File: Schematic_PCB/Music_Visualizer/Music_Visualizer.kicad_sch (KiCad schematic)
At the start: 130 parts, among them U1 LM324, U4 LM324, U5 LM324, U6 LM324, U7 LM324, U8 LM324, U9 LM324

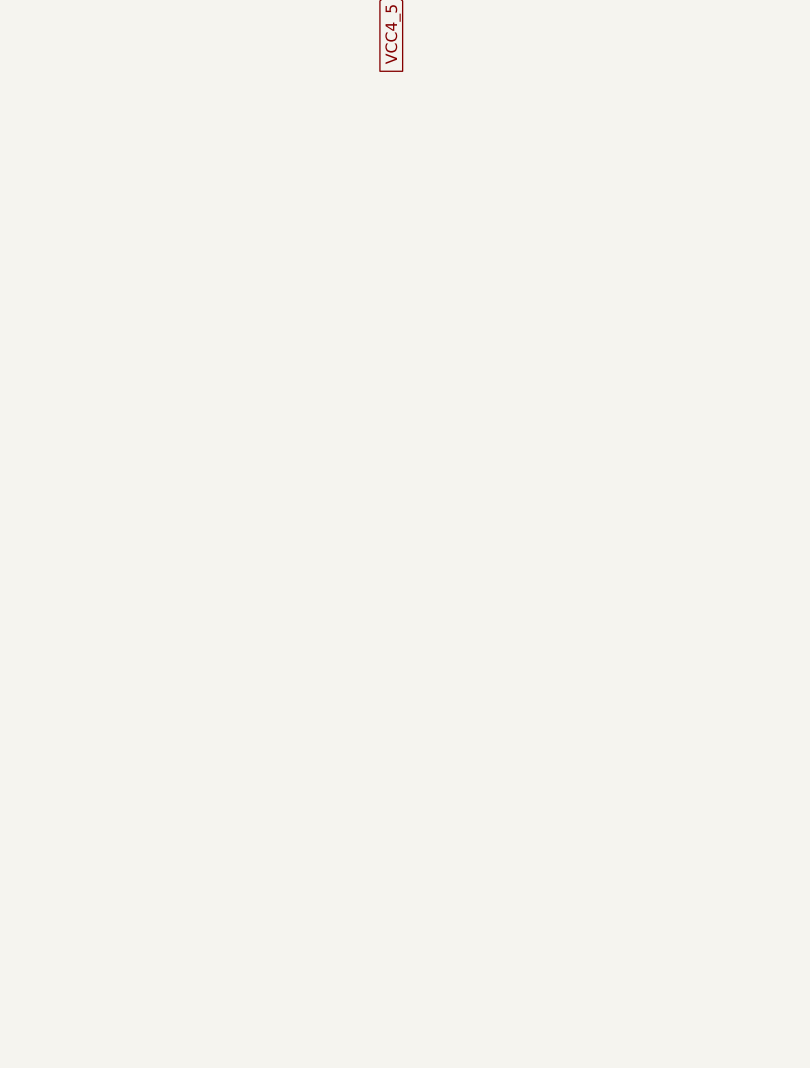
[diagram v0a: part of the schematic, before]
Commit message: Add testpoints
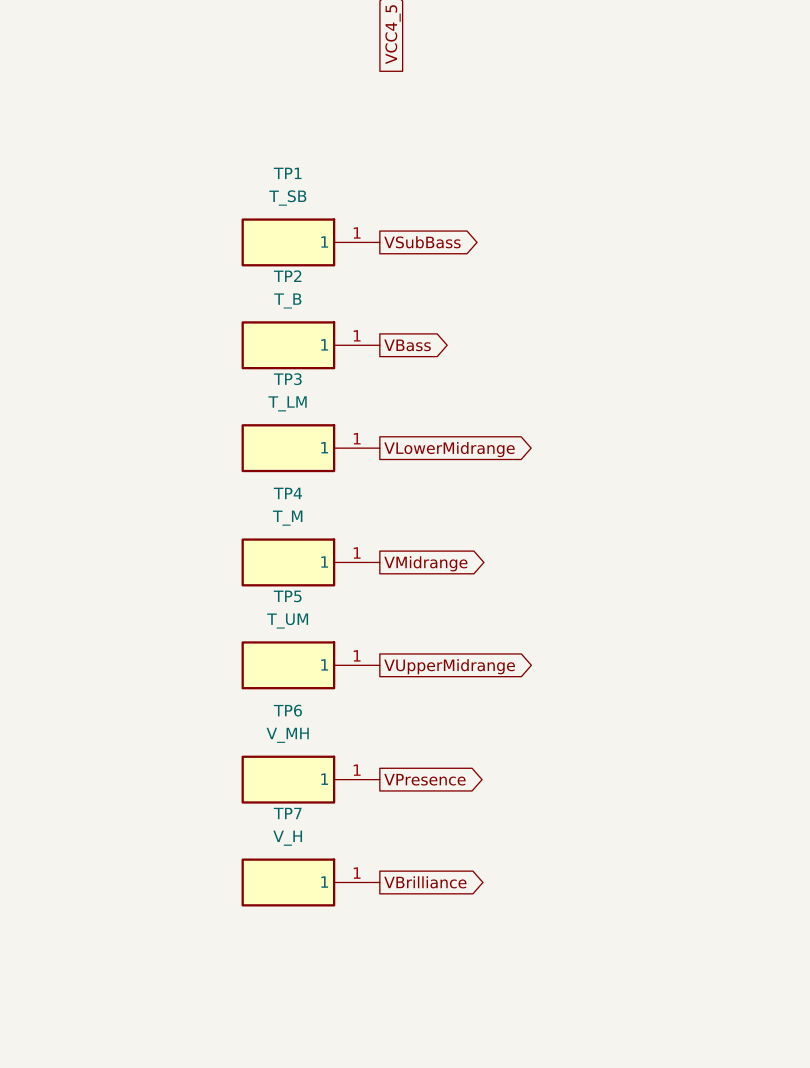
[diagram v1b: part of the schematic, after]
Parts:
- added TP1: T_SB, Custom_Footprints:TEST1Y, symbol TEST-1_Y_:TEST-1_Y_
- added TP2: T_B, Custom_Footprints:TEST1Y, symbol TEST-1_Y_:TEST-1_Y_
- added TP3: T_LM, Custom_Footprints:TEST1Y, symbol TEST-1_Y_:TEST-1_Y_
- added TP4: T_M, Custom_Footprints:TEST1Y, symbol TEST-1_Y_:TEST-1_Y_
- added TP5: T_UM, Custom_Footprints:TEST1Y, symbol TEST-1_Y_:TEST-1_Y_
- added TP6: V_MH, Custom_Footprints:TEST1Y, symbol TEST-1_Y_:TEST-1_Y_
- added TP7: V_H, Custom_Footprints:TEST1Y, symbol TEST-1_Y_:TEST-1_Y_
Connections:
- net VBass: now also TP2.1
- net VBrilliance: now also TP7.1
- net VLowerMidrange: now also TP3.1
- net VMidrange: now also TP4.1
- net VPresence: now also TP6.1
- net VSubBass: now also TP1.1
- net VUpperMidrange: now also TP5.1

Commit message: Correct op amps
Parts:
- renumbered U4 to U2, U5 to U3, U6 to U4, U7 to U5, U8 to U6, U9 to U7
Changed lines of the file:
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@@
 		(dnp no)
 		(fields_autoplaced yes)
-		(property "Reference" "U4"
+		(property "Reference" "U2"
 			(at 39.37 116.84 0)
 			(effects
@@
 			)
 		)
-		(property "Sim.Pins" "12=1 13=2 14=3"
+		(property "Sim.Pins" "8=1 9=2 10=3"
 			(at -12.7 78.74 0)
 			(effects
@@
 			(project "Music_Visualizer"
 				(path "/236ff8a0-79ed-4eaf-ae36-90444797fa8d"
-					(reference "U4")
+					(reference "U2")
 					(unit 4)
 				)
@@
 		(dnp no)
 		(fields_autoplaced yes)
-		(property "Reference" "U6"
+		(property "Reference" "U4"
 			(at 41.91 260.35 0)
 			(effects
@@
 			)
 		)
-		(property "Sim.Pins" "12=1 13=2 14=3"
+		(property "Sim.Pins" "8=1 9=2 10=3"
 			(at -10.16 222.25 0)
 			(effects
@@
 			(project "Music_Visualizer"
 				(path "/236ff8a0-79ed-4eaf-ae36-90444797fa8d"
-					(reference "U6")
+					(reference "U4")
 					(unit 4)
 				)
@@
 		(on_board yes)
 		(dnp no)
-		(property "Reference" "U7"
+		(property "Reference" "U5"
 			(at 458.47 66.04 0)
 			(effects
@@
 			(project "Music_Visualizer"
 				(path "/236ff8a0-79ed-4eaf-ae36-90444797fa8d"
-					(reference "U7")
+					(reference "U5")
 					(unit 3)
 				)
@@
 		(dnp no)
 		(fields_autoplaced yes)
-		(property "Reference" "U8"
+		(property "Reference" "U6"
 			(at 406.4 120.65 0)
 			(effects
@@
 			(project "Music_Visualizer"
 				(path "/236ff8a0-79ed-4eaf-ae36-90444797fa8d"
-					(reference "U8")
+					(reference "U6")
 					(unit 2)
 				)
@@
 		(on_board yes)
 		(dnp no)
-		(property "Reference" "U5"
+		(property "Reference" "U3"
 			(at 195.58 209.55 0)
 			(effects
@@
 			(project "Music_Visualizer"
 				(path "/236ff8a0-79ed-4eaf-ae36-90444797fa8d"
-					(reference "U5")
+					(reference "U3")
 					(unit 3)
 				)
@@
 		(on_board yes)
 		(dnp no)
-		(property "Reference" "U6"
+		(property "Reference" "U4"
 			(at 198.12 283.21 0)
 			(effects
@@
 			(project "Music_Visualizer"
 				(path "/236ff8a0-79ed-4eaf-ae36-90444797fa8d"
-					(reference "U6")
+					(reference "U4")
 					(unit 3)
 				)
@@
 		(on_board yes)
 		(dnp no)
-		(property "Reference" "U9"
+		(property "Reference" "U7"
 			(at 457.2 214.63 0)
 			(effects
@@
 			(project "Music_Visualizer"
 				(path "/236ff8a0-79ed-4eaf-ae36-90444797fa8d"
-					(reference "U9")
+					(reference "U7")
 					(unit 3)
 				)
@@
 		(dnp no)
 		(fields_autoplaced yes)
-		(property "Reference" "U7"
+		(property "Reference" "U5"
 			(at 302.26 43.18 0)
 			(effects
@@
 			)
 		)
-		(property "Sim.Pins" "12=1 13=2 14=3"
+		(property "Sim.Pins" "8=1 9=2 10=3"
 			(at 250.19 5.08 0)
 			(effects
@@
 			(project "Music_Visualizer"
 				(path "/236ff8a0-79ed-4eaf-ae36-90444797fa8d"
-					(reference "U7")
+					(reference "U5")
 					(unit 4)
 				)
@@
 		(dnp no)
 		(fields_autoplaced yes)
-		(property "Reference" "U7"
+		(property "Reference" "U5"
 			(at 407.67 45.72 0)
 			(effects
@@
 			)
 		)
-		(property "Sim.Pins" "5=1 6=2 7=3"
+		(property "Sim.Pins" "8=1 9=2 10=3"
 			(at 251.46 5.08 0)
 			(effects
@@
 			(project "Music_Visualizer"
 				(path "/236ff8a0-79ed-4eaf-ae36-90444797fa8d"
-					(reference "U7")
+					(reference "U5")
 					(unit 2)
 				)
@@
 		(dnp no)
 		(fields_autoplaced yes)
-		(property "Reference" "U9"
+		(property "Reference" "U7"
 			(at 300.99 191.77 0)
 			(effects
@@
 			)
 		)
-		(property "Sim.Pins" "12=1 13=2 14=3"
+		(property "Sim.Pins" "8=1 9=2 10=3"
 			(at 248.92 153.67 0)
 			(effects
@@
 			(project "Music_Visualizer"
 				(path "/236ff8a0-79ed-4eaf-ae36-90444797fa8d"
-					(reference "U9")
+					(reference "U7")
 					(unit 4)
 				)
@@
 		(on_board yes)
 		(dnp no)
-		(property "Reference" "U4"
+		(property "Reference" "U2"
 			(at 195.58 139.7 0)
 			(effects
@@
 			(project "Music_Visualizer"
 				(path "/236ff8a0-79ed-4eaf-ae36-90444797fa8d"
-					(reference "U4")
+					(reference "U2")
 					(unit 3)
 				)
@@
 		(on_board yes)
 		(dnp no)
-		(property "Reference" "U8"
+		(property "Reference" "U6"
 			(at 457.2 140.97 0)
 			(effects
@@
 			)
 		)
-		(property "Sim.Pins" "8=1 9=2 10=3"
+		(property "Sim.Pins" "5=1 6=2 7=3"
 			(at 250.19 80.01 0)
 			(effects
@@
 			(project "Music_Visualizer"
 				(path "/236ff8a0-79ed-4eaf-ae36-90444797fa8d"
-					(reference "U8")
+					(reference "U6")
 					(unit 3)
 				)
@@
 		(dnp no)
 		(fields_autoplaced yes)
-		(property "Reference" "U4"
+		(property "Reference" "U2"
 			(at 144.78 119.38 0)
 			(effects
@@
 			)
 		)
-		(property "Sim.Pins" "5=1 6=2 7=3"
+		(property "Sim.Pins" "8=1 9=2 10=3"
 			(at -11.43 78.74 0)
 			(effects
@@
 			(project "Music_Visualizer"
 				(path "/236ff8a0-79ed-4eaf-ae36-90444797fa8d"
-					(reference "U4")
+					(reference "U2")
 					(unit 2)
 				)
@@
 		(dnp no)
 		(fields_autoplaced yes)
-		(property "Reference" "U6"
+		(property "Reference" "U4"
 			(at 147.32 262.89 0)
 			(effects
@@
 			)
 		)
-		(property "Sim.Pins" "5=1 6=2 7=3"
+		(property "Sim.Pins" "8=1 9=2 10=3"
 			(at -8.89 222.25 0)
 			(effects
@@
 			(project "Music_Visualizer"
 				(path "/236ff8a0-79ed-4eaf-ae36-90444797fa8d"
-					(reference "U6")
+					(reference "U4")
 					(unit 2)
 				)
@@
 		(dnp no)
 		(fields_autoplaced yes)
-		(property "Reference" "U6"
+		(property "Reference" "U4"
 			(at 97.79 262.89 0)
 			(effects
@@
 			)
 		)
-		(property "Sim.Pins" "1=1 2=2 3=3"
+		(property "Sim.Pins" "8=1 9=2 10=3"
 			(at -8.89 222.25 0)
 			(effects
@@
 			(project "Music_Visualizer"
 				(path "/236ff8a0-79ed-4eaf-ae36-90444797fa8d"
-					(reference "U6")
+					(reference "U4")
 					(unit 1)
 				)
@@
 		(dnp no)
 		(fields_autoplaced yes)
-		(property "Reference" "U5"
+		(property "Reference" "U3"
 			(at 95.25 189.23 0)
 			(effects
@@
 			)
 		)
-		(property "Sim.Pins" "1=1 2=2 3=3"
+		(property "Sim.Pins" "8=1 9=2 10=3"
 			(at -11.43 148.59 0)
 			(effects
@@
 			(project "Music_Visualizer"
 				(path "/236ff8a0-79ed-4eaf-ae36-90444797fa8d"
-					(reference "U5")
+					(reference "U3")
 					(unit 1)
 				)
@@
 		(dnp no)
 		(fields_autoplaced yes)
-		(property "Reference" "U9"
+		(property "Reference" "U7"
 			(at 356.87 194.31 0)
 			(effects
@@
 			)
 		)
-		(property "Sim.Pins" "1=1 2=2 3=3"
+		(property "Sim.Pins" "8=1 9=2 10=3"
 			(at 250.19 153.67 0)
 			(effects
@@
 			(project "Music_Visualizer"
 				(path "/236ff8a0-79ed-4eaf-ae36-90444797fa8d"
-					(reference "U9")
+					(reference "U7")
 					(unit 1)
 				)
@@
 		(dnp no)
 		(fields_autoplaced yes)
-		(property "Reference" "U7"
+		(property "Reference" "U5"
 			(at 358.14 45.72 0)
 			(effects
@@
 			)
 		)
-		(property "Sim.Pins" "1=1 2=2 3=3"
+		(property "Sim.Pins" "8=1 9=2 10=3"
 			(at 251.46 5.08 0)
 			(effects
@@
 			(project "Music_Visualizer"
 				(path "/236ff8a0-79ed-4eaf-ae36-90444797fa8d"
-					(reference "U7")
+					(reference "U5")
 					(unit 1)
 				)
@@
 		(dnp no)
 		(fields_autoplaced yes)
-		(property "Reference" "U5"
+		(property "Reference" "U3"
 			(at 39.37 186.69 0)
 			(effects
@@
 			)
 		)
-		(property "Sim.Pins" "12=1 13=2 14=3"
+		(property "Sim.Pins" "8=1 9=2 10=3"
 			(at -12.7 148.59 0)
 			(effects
@@
 			(project "Music_Visualizer"
 				(path "/236ff8a0-79ed-4eaf-ae36-90444797fa8d"
-					(reference "U5")
+					(reference "U3")
 					(unit 4)
 				)
@@
 		(dnp no)
 		(fields_autoplaced yes)
-		(property "Reference" "U8"
+		(property "Reference" "U6"
 			(at 300.99 118.11 0)
 			(effects
@@
 			)
 		)
-		(property "Sim.Pins" "12=1 13=2 14=3"
+		(property "Sim.Pins" "5=1 6=2 7=3"
 			(at 248.92 80.01 0)
 			(effects
@@
 			(project "Music_Visualizer"
 				(path "/236ff8a0-79ed-4eaf-ae36-90444797fa8d"
-					(reference "U8")
+					(reference "U6")
 					(unit 4)
 				)
@@
 		(dnp no)
 		(fields_autoplaced yes)
-		(property "Reference" "U9"
+		(property "Reference" "U7"
 			(at 406.4 194.31 0)
 			(effects
@@
 			)
 		)
-		(property "Sim.Pins" "5=1 6=2 7=3"
+		(property "Sim.Pins" "8=1 9=2 10=3"
 			(at 250.19 153.67 0)
 			(effects
@@
 			(project "Music_Visualizer"
 				(path "/236ff8a0-79ed-4eaf-ae36-90444797fa8d"
-					(reference "U9")
+					(reference "U7")
 					(unit 2)
 				)
@@
 		(dnp no)
 		(fields_autoplaced yes)
-		(property "Reference" "U5"
+		(property "Reference" "U3"
 			(at 144.78 189.23 0)
 			(effects
@@
 			)
 		)
-		(property "Sim.Pins" "5=1 6=2 7=3"
+		(property "Sim.Pins" "8=1 9=2 10=3"
 			(at -11.43 148.59 0)
 			(effects
@@
 			(project "Music_Visualizer"
 				(path "/236ff8a0-79ed-4eaf-ae36-90444797fa8d"
-					(reference "U5")
+					(reference "U3")
 					(unit 2)
 				)
@@
 		(dnp no)
 		(fields_autoplaced yes)
-		(property "Reference" "U4"
+		(property "Reference" "U2"
 			(at 95.25 119.38 0)
 			(effects
@@
 			)
 		)
-		(property "Sim.Pins" "1=1 2=2 3=3"
+		(property "Sim.Pins" "8=1 9=2 10=3"
 			(at -11.43 78.74 0)
 			(effects
@@
 			(project "Music_Visualizer"
 				(path "/236ff8a0-79ed-4eaf-ae36-90444797fa8d"
-					(reference "U4")
+					(reference "U2")
 					(unit 1)
 				)
@@
 		(dnp no)
 		(fields_autoplaced yes)
-		(property "Reference" "U8"
+		(property "Reference" "U6"
 			(at 356.87 120.65 0)
 			(effects
@@
 			)
 		)
-		(property "Sim.Pins" "1=1 2=2 3=3"
+		(property "Sim.Pins" "5=1 6=2 7=3"
 			(at 250.19 80.01 0)
 			(effects
@@
 			(project "Music_Visualizer"
 				(path "/236ff8a0-79ed-4eaf-ae36-90444797fa8d"
-					(reference "U8")
+					(reference "U6")
 					(unit 1)
 				)

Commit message: PCB V1 done
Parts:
- C1, C11, C12, C13, C14, C15, C16, C18, C19, C2, C20, C21, C22, C23, C25, C26, C27, C28, C29, C3, C30, C31, C32, C33, C34, C35, C36, C37, C38, C39, C4, C40, C41, C42, C44, C45, C46, C47, C48, C49, C5, C50, C51, C52, C53, C6: footprint Capacitor_SMD:C_0805_2012Metric_Pad1.18x1.45mm_HandSolder -> Custom_Footprints:C_0805_2012Metric_Pad1.18x1.45mm_HandSolder
- R1, R13, R14, R15, R16, R17, R18, R19, R2, R20, R21, R22, R23, R24, R25, R26, R27, R28, R29, R3, R30, R31, R32, R33, R34, R35, R36, R37, R38, R39, R4, R40, R41, R42, R43, R44, R45, R46, R47, R48, R49, R5, R50, R51, R52, R53, R54, R55, R56, R57, R58, R59, R6, R60, R61, R62, R63, R64, R65, R66, R67, R68, R69, R7, R70, R71, R72, R73, R8, R9: footprint Resistor_SMD:R_0805_2012Metric_Pad1.20x1.40mm_HandSolder -> Custom_Footprints:R_0805_2012Metric_Pad1.20x1.40mm_HandSolder

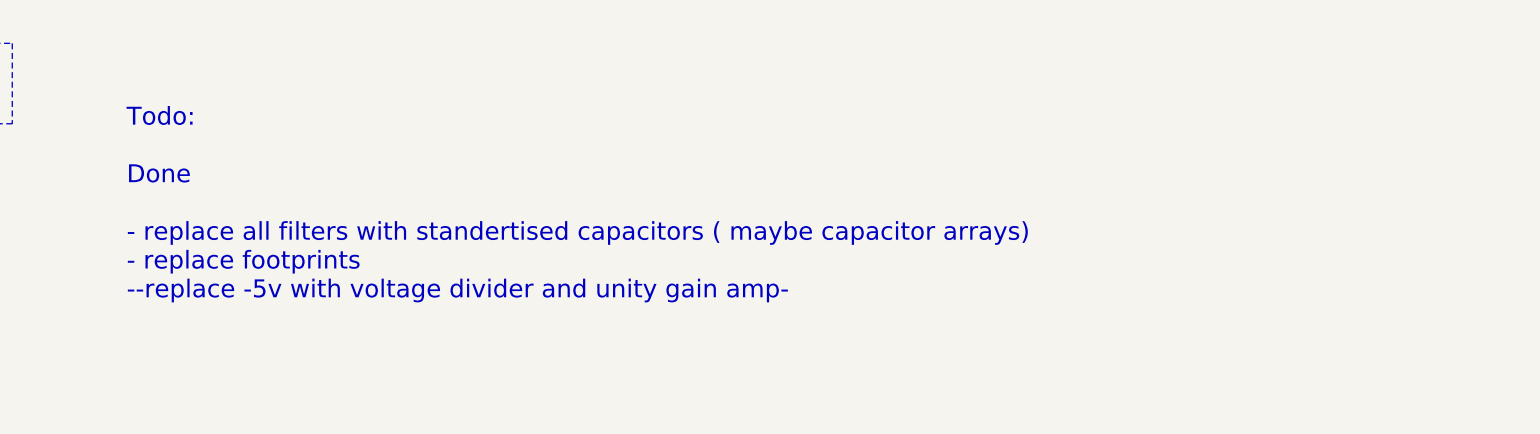
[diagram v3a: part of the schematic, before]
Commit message: Chnge diode footprint to 1206
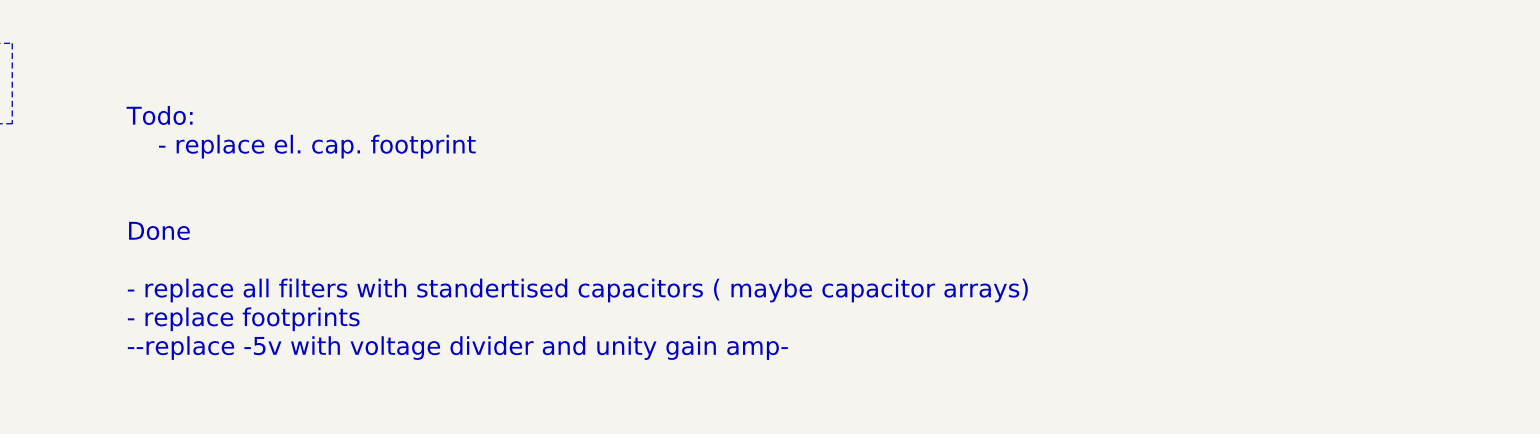
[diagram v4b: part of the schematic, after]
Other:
- note added: "Todo: - replace el. cap. footprint Done - replace all filters with standertised capacitors ( maybe capacitor arrays) - replace footprints --replace -5v with voltage divider and unity gain amp-"
- note removed: "Todo: Done - replace all filters with standertised capacitors ( maybe capacitor arrays) - replace footprints --replace -5v with voltage divider and unity gain amp-"
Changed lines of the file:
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@@
 		)
 	)
-	(text "Todo:\n\nDone\n\n- replace all filters with standertised capacitors ( maybe capacitor arrays)\n- replace footprints\n--replace -5v with voltage divider and unity gain amp-"
+	(text "Todo:\n	- replace el. cap. footprint\n\n\nDone\n\n- replace all filters with standertised capacitors ( maybe capacitor arrays)\n- replace footprints\n--replace -5v with voltage divider and unity gain amp-"
 		(exclude_from_sim no)
 		(at 182.626 359.664 0)

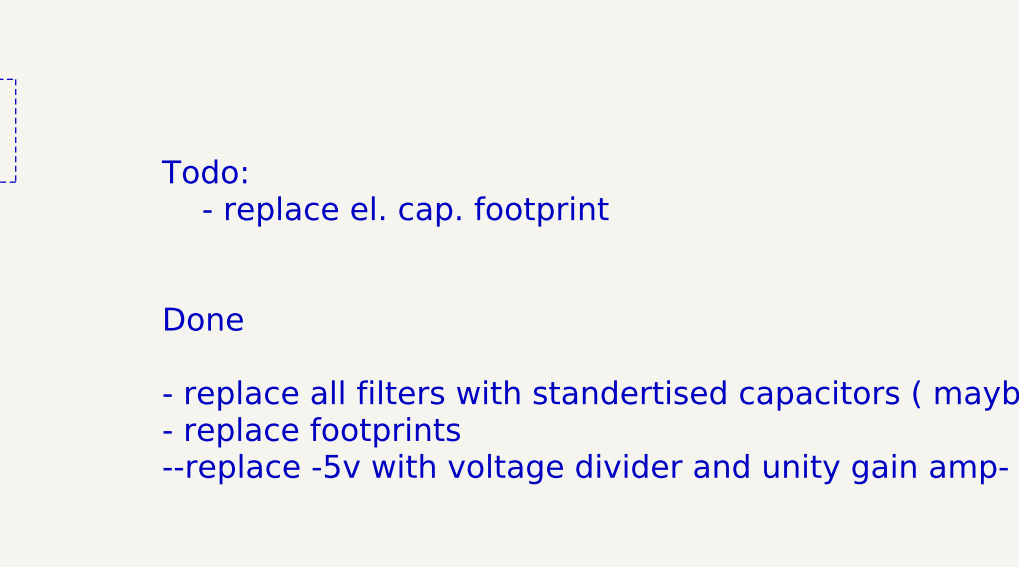
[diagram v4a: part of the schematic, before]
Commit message: Replace elec. cap.
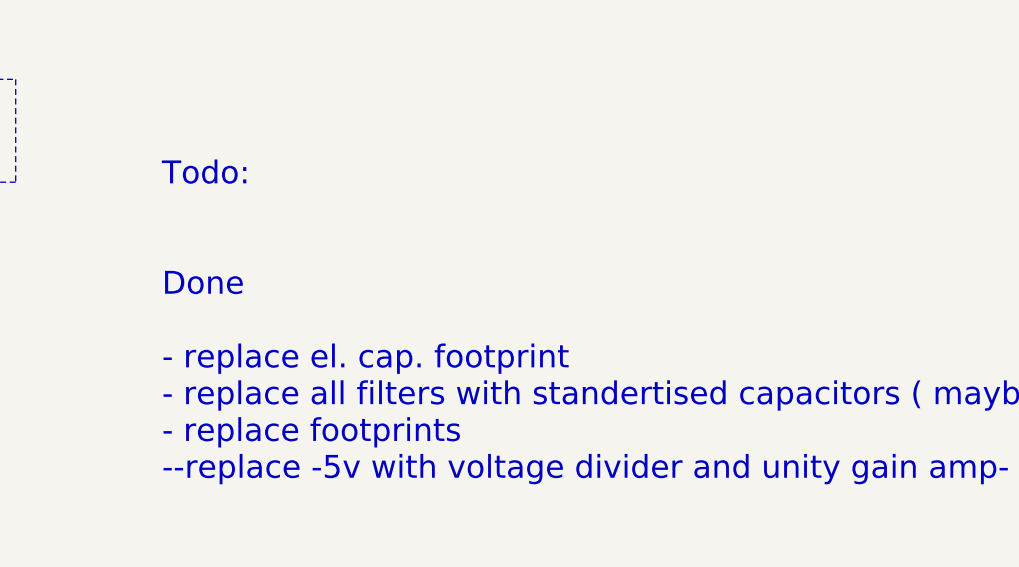
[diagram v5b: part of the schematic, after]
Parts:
- C17, C24, C43: footprint Capacitor_SMD:C_0805_2012Metric_Pad1.18x1.45mm_HandSolder -> Capacitor_SMD:CP_Elec_4x5.4
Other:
- note added: "Todo: Done - replace el. cap. footprint - replace all filters with standertised capacitors ( maybe capacitor arrays) - replace footprints --replace -5v with voltage divider and unity gain amp-"
- note removed: "Todo: - replace el. cap. footprint Done - replace all filters with standertised capacitors ( maybe capacitor arrays) - replace footprints --replace -5v with voltage divider and unity gain amp-"
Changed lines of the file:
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@@
 		)
 	)
-	(text "Todo:\n	- replace el. cap. footprint\n\n\nDone\n\n- replace all filters with standertised capacitors ( maybe capacitor arrays)\n- replace footprints\n--replace -5v with voltage divider and unity gain amp-"
+	(text "Todo:\n\n\nDone\n\n- replace el. cap. footprint\n- replace all filters with standertised capacitors ( maybe capacitor arrays)\n- replace footprints\n--replace -5v with voltage divider and unity gain amp-"
 		(exclude_from_sim no)
 		(at 182.626 359.664 0)
@@
 			)
 		)
-		(property "Footprint" "Capacitor_SMD:C_0805_2012Metric_Pad1.18x1.45mm_HandSolder"
+		(property "Footprint" "Capacitor_SMD:CP_Elec_4x5.4"
 			(at 213.36 183.1848 0)
 			(effects
@@
 			)
 		)
-		(property "Footprint" "Capacitor_SMD:C_0805_2012Metric_Pad1.18x1.45mm_HandSolder"
+		(property "Footprint" "Capacitor_SMD:CP_Elec_4x5.4"
 			(at 213.36 113.3348 0)
 			(effects
@@
 			)
 		)
-		(property "Footprint" "Capacitor_SMD:C_0805_2012Metric_Pad1.18x1.45mm_HandSolder"
+		(property "Footprint" "Capacitor_SMD:CP_Elec_4x5.4"
 			(at 224.79 46.0248 0)
 			(effects
